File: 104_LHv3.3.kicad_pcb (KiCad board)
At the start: 2 copper layers, 436.9 x 129.9 mm, 229 parts, among them K1 CHRY_MX, K10 CHRY_MX, K100 CHRY_MX, K101 CHRY_MX, K102 CHRY_MX, K103 CHRY_MX, K104 CHRY_MX, K11 CHRY_MX, K12 CHRY_MX, K13 CHRY_MX, K14 CHRY_MX, K15 CHRY_MX, K16 CHRY_MX, K17 CHRY_MX, K18 CHRY_MX, K19 CHRY_MX, K2 CHRY_MX, K20 CHRY_MX, K21 CHRY_MX, K22 CHRY_MX, K23 CHRY_MX, K24 CHRY_MX, K25 CHRY_MX, K26 CHRY_MX, K27 CHRY_MX, K28 CHRY_MX, K29 CHRY_MX, K3 CHRY_MX, K30 CHRY_MX, K31 CHRY_MX, K32 CHRY_MX, K33 CHRY_MX, K34 CHRY_MX, K35 CHRY_MX, K36 CHRY_MX, K37 CHRY_MX, K38 CHRY_MX, K39 CHRY_MX, K4 CHRY_MX, K40 CHRY_MX, K41 CHRY_MX, K42 CHRY_MX, K43 CHRY_MX, K44 CHRY_MX, K45 CHRY_MX, K46 CHRY_MX, K47 CHRY_MX, K48 CHRY_MX, K49 CHRY_MX, K5 CHRY_MX, K50 CHRY_MX, K51 CHRY_MX, K52 CHRY_MX, K53 CHRY_MX, K54 CHRY_MX, K55 CHRY_MX, K56 CHRY_MX, K57 CHRY_MX, K58 CHRY_MX, K59 CHRY_MX, K6 CHRY_MX, K60 CHRY_MX, K61 CHRY_MX, K62 CHRY_MX, K63 CHRY_MX, K64 CHRY_MX, K65 CHRY_MX, K66 CHRY_MX, K67 CHRY_MX, K68 CHRY_MX, K69 CHRY_MX, K7 CHRY_MX, K70 CHRY_MX, K71 CHRY_MX, K72 CHRY_MX, K73 CHRY_MX, K74 CHRY_MX, K75 CHRY_MX, K76 CHRY_MX, K77 CHRY_MX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

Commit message: Add files via upload
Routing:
- net /COL_10: track 371.0 -> 348.4 mm
- net /SELECT: track 169.8 -> 152.6 mm, vias 2 -> 4
- net /COL_04: track 185.0 -> 177.8 mm
- net /GND: track 366.3 -> 359.1 mm, vias 33 -> 32
- net /COL_13: track 390.6 -> 384.7 mm
- net /COL_17: track 459.2 -> 464.9 mm
- net /COL_16: track 422.6 -> 427.0 mm
- net /ROW_04: track 510.4 -> 506.4 mm
- net /COL_05: track 191.2 -> 193.3 mm
- net /COL_14: track 397.7 -> 399.5 mm
- net /COL_21: track 531.0 -> 532.7 mm
- net /COL_20: track 525.6 -> 527.2 mm
- net /COL_19: track 459.1 -> 460.3 mm
- net /COL_07: track 256.6 -> 257.8 mm
- net /COL_15: track 420.8 -> 419.8 mm
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
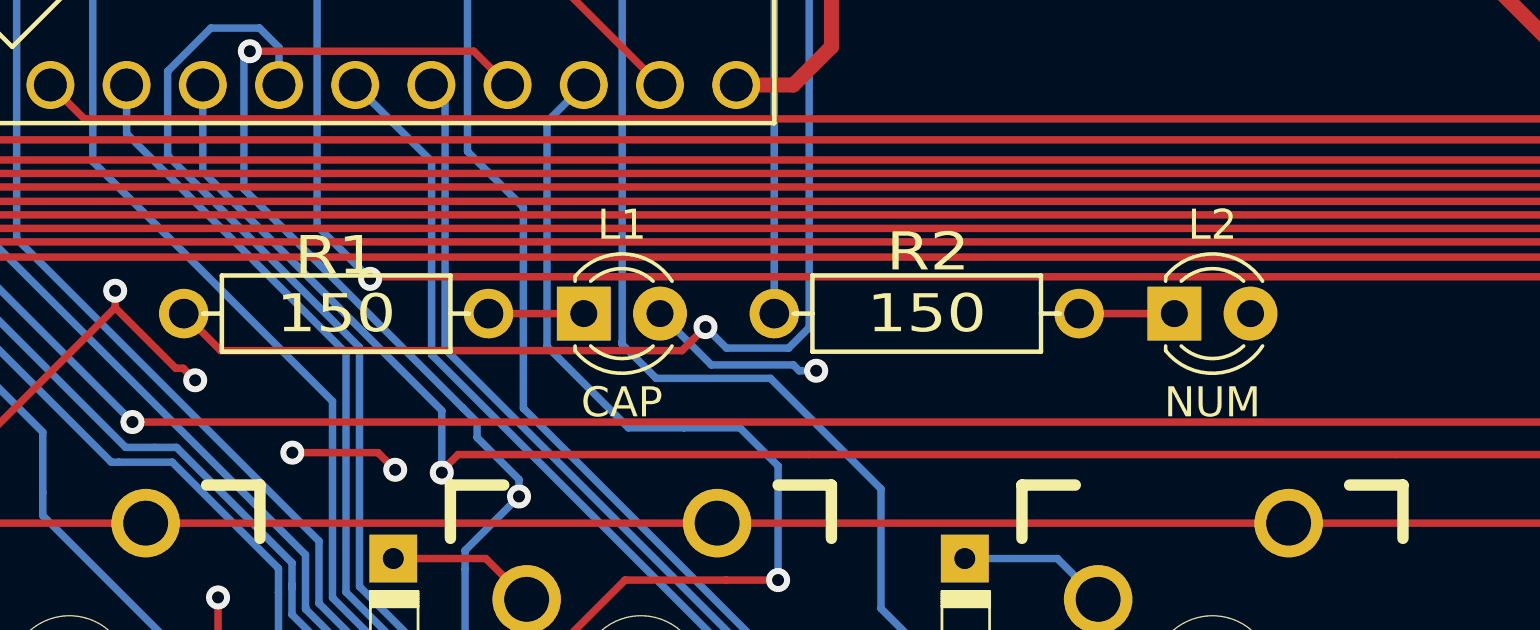
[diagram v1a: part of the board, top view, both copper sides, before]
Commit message: Fixed backwards LEDs
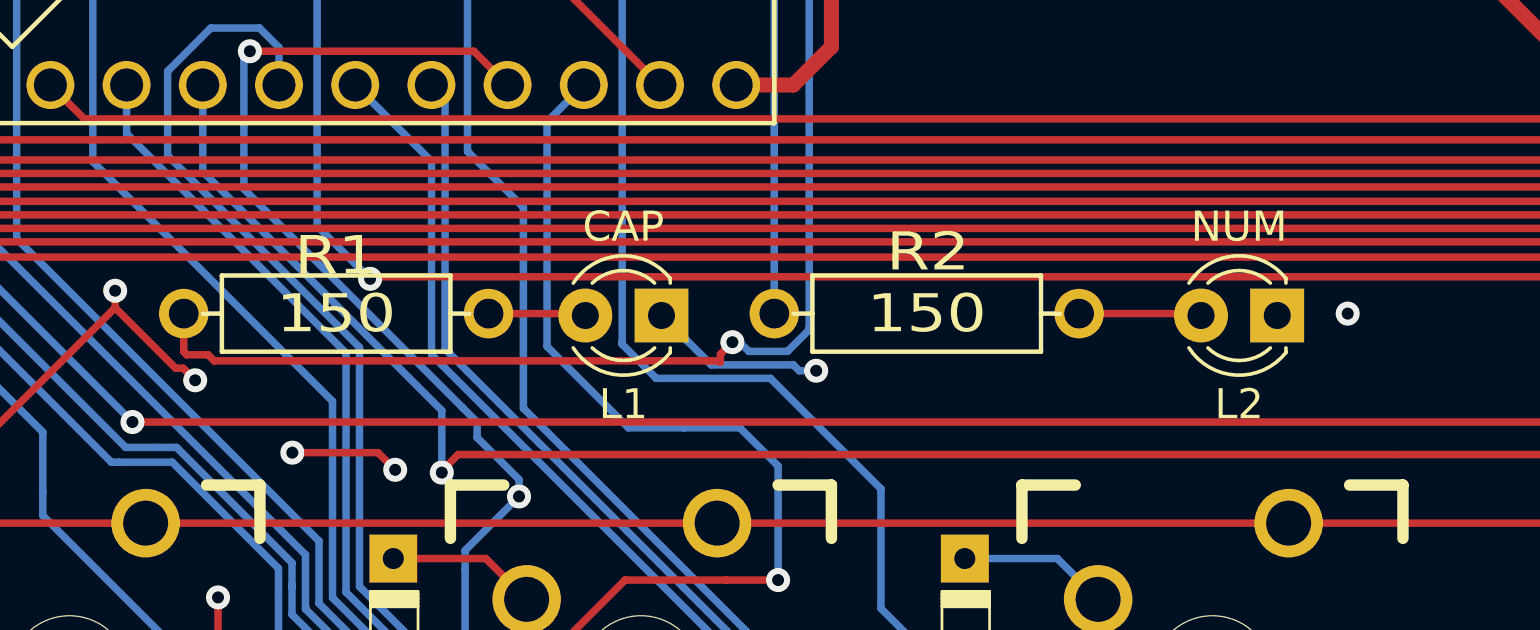
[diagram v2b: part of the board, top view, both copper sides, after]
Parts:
- moved L2 3.43 mm to (127.9, 109.3), turned to 180 degrees
- moved L1 2.59 mm to (107.4, 109.3), turned to 180 degrees
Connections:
- L1 pad 1: /R1 -> /GND
- L1 pad 2: /GND -> /R1
- L2 pad 1: /R2 -> /GND
- L2 pad 2: /GND -> /R2
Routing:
- net /LED_00: track 47.6 -> 48.6 mm
- net /GND: vias 32 -> 33
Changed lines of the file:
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@@
     (thickness 1.6)
     (drawings 43)
-    (tracks 1490)
+    (tracks 1498)
     (zones 0)
     (modules 229)
@@
   )
   (module pcb:LED_D3.0mm_FlatTop (layer F.Cu)
-    (at 124.46 109.22)
+    (at 127.889 109.2835 180)
     (descr "LED, Round, FlatTop, diameter 3.0mm, 2 pins, http://www.kingbright.com/attachments/file/psearch/000/00/00/L-47XEC(Ver.9A).pdf")
     (tags "LED Round FlatTop diameter 3.0mm 2 pins")
-    (fp_text reference L2 (at 1.27 -2.96) (layer F.SilkS)
+    (fp_text reference L2 (at 1.27 -2.96 180) (layer F.SilkS)
       (effects (font (size 1 1) (thickness 0.15)))
     )
-    (fp_text value NUM (at 1.27 2.96) (layer F.SilkS)
+    (fp_text value NUM (at 1.27 2.96 180) (layer F.SilkS)
       (effects (font (size 1 1) (thickness 0.15)))
     )
@@
     (fp_line (start 3.7 2.25) (end 3.7 -2.25) (layer F.CrtYd) (width 0.05))
     (fp_line (start 3.7 -2.25) (end -1.15 -2.25) (layer F.CrtYd) (width 0.05))
-    (pad 1 thru_hole rect (at 0 0) (size 1.8 1.8) (drill 0.9) (layers *.Cu *.Mask)
-      (net 141 /R2))
-    (pad 2 thru_hole circle (at 2.54 0) (size 1.8 1.8) (drill 0.9) (layers *.Cu *.Mask)
+    (pad 1 thru_hole rect (at 0 0 180) (size 1.8 1.8) (drill 0.9) (layers *.Cu *.Mask)
       (net 127 /GND))
+    (pad 2 thru_hole circle (at 2.54 0 180) (size 1.8 1.8) (drill 0.9) (layers *.Cu *.Mask)
+      (net 141 /R2))
   )
   (module pcb:LED_D3.0mm_FlatTop (layer F.Cu)
-    (at 104.775 109.22)
+    (at 107.3658 109.2835 180)
     (descr "LED, Round, FlatTop, diameter 3.0mm, 2 pins, http://www.kingbright.com/attachments/file/psearch/000/00/00/L-47XEC(Ver.9A).pdf")
     (tags "LED Round FlatTop diameter 3.0mm 2 pins")
-    (fp_text reference L1 (at 1.27 -2.96) (layer F.SilkS)
+    (fp_text reference L1 (at 1.27 -2.96 180) (layer F.SilkS)
       (effects (font (size 1 1) (thickness 0.15)))
     )
-    (fp_text value CAP (at 1.27 2.96) (layer F.SilkS)
+    (fp_text value CAP (at 1.27 2.96 180) (layer F.SilkS)
       (effects (font (size 1 1) (thickness 0.15)))
     )
@@
     (fp_arc (start 1.27 0) (end -0.29 -1.235516) (angle 108.8) (layer F.SilkS) (width 0.12))
     (fp_arc (start 1.27 0) (end -0.23 -1.16619) (angle 284.3) (layer F.Fab) (width 0.1))
-    (pad 2 thru_hole circle (at 2.54 0) (size 1.8 1.8) (drill 0.9) (layers *.Cu *.Mask)
-      (net 127 /GND))
-    (pad 1 thru_hole rect (at 0 0) (size 1.8 1.8) (drill 0.9) (layers *.Cu *.Mask)
+    (pad 2 thru_hole circle (at 2.54 0 180) (size 1.8 1.8) (drill 0.9) (layers *.Cu *.Mask)
       (net 140 /R1))
+    (pad 1 thru_hole rect (at 0 0 180) (size 1.8 1.8) (drill 0.9) (layers *.Cu *.Mask)
+      (net 127 /GND))
   )
   (module pcb:RESISTOR (layer F.Cu)
@@
   (gr_line (start 131.192 77.78) (end 121.868 77.78) (layer Edge.Cuts) (width 0.15))
   (gr_arc (start 134.73 83.33) (end 131.98 83.33) (angle -180) (layer Edge.Cuts) (width 0.15))
+  (via (at 130.2385 109.22) (size 0.8) (drill 0.4) (layers F.Cu B.Cu) (net 127))
   (segment (start 138.2724 102.7298) (end 138.2366 102.694) (width 0.25) (layer B.Cu) (net 1))
   (segment (start 144.78 97.245) (end 143.7572 97.245) (width 0.25) (layer B.Cu) (net 1))
@@
   (segment (start 107.315 86.36) (end 112.2874 91.3324) (width 0.25) (layer B.Cu) (net 143))
   (segment (start 112.2874 91.3324) (end 112.2874 109.6852) (width 0.25) (layer B.Cu) (net 143))
-  (segment (start 112.2874 109.6852) (end 111.6018 110.3708) (width 0.25) (layer B.Cu) (net 143))
-  (segment (start 111.6018 110.3708) (end 109.5324 110.3708) (width 0.25) (layer B.Cu) (net 143))
-  (segment (start 109.5324 110.3708) (end 108.8312 109.6696) (width 0.25) (layer B.Cu) (net 143))
-  (segment (start 108.8312 109.6696) (end 108.0469 110.4539) (width 0.25) (layer F.Cu) (net 143))
-  (segment (start 108.0469 110.4539) (end 92.6739 110.4539) (width 0.25) (layer F.Cu) (net 143))
-  (segment (start 92.6739 110.4539) (end 91.44 109.22) (width 0.25) (layer F.Cu) (net 143))
-  (via (at 108.8312 109.6696) (size 0.8) (layers F.Cu B.Cu) (net 143))
+  (via (at 109.728 110.1725) (size 0.8) (layers F.Cu B.Cu) (net 143))
+  (segment (start 112.2874 109.760342) (end 111.568762 110.47898) (width 0.25) (layer B.Cu) (net 143))
+  (segment (start 112.2874 109.6852) (end 112.2874 109.760342) (width 0.25) (layer B.Cu) (net 143))
+  (segment (start 109.728 110.1725) (end 109.9693 110.1725) (width 0.25) (layer B.Cu) (net 143))
+  (segment (start 109.9693 110.1725) (end 110.27578 110.47898) (width 0.25) (layer B.Cu) (net 143))
+  (segment (start 110.27578 110.47898) (end 111.5568 110.47898) (width 0.25) (layer B.Cu) (net 143))
+  (segment (start 109.328001 110.572499) (end 109.328001 110.839199) (width 0.25) (layer F.Cu) (net 143))
+  (segment (start 109.728 110.1725) (end 109.328001 110.572499) (width 0.25) (layer F.Cu) (net 143))
+  (segment (start 109.328001 110.839199) (end 109.283602 110.7948) (width 0.25) (layer F.Cu) (net 143))
+  (segment (start 109.283602 110.7948) (end 92.456 110.7948) (width 0.25) (layer F.Cu) (net 143))
+  (segment (start 92.253692 110.592492) (end 91.542492 110.592492) (width 0.25) (layer F.Cu) (net 143))
+  (segment (start 92.456 110.7948) (end 92.253692 110.592492) (width 0.25) (layer F.Cu) (net 143))
+  (segment (start 91.542492 110.592492) (end 91.44 110.49) (width 0.25) (layer F.Cu) (net 143))
+  (segment (start 91.44 110.49) (end 91.44 109.22) (width 0.25) (layer F.Cu) (net 143))
   (segment (start 104.775 86.36) (end 111.125 92.71) (width 0.25) (layer B.Cu) (net 144))
   (segment (start 111.125 92.71) (end 111.125 109.22) (width 0.25) (layer B.Cu) (net 144))

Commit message: Clean up LED text
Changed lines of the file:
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@@
   )
   (layers
-    (0 F.Cu signal)
-    (31 B.Cu signal)
+    (0 F.Cu signal hide)
+    (31 B.Cu signal hide)
     (32 B.Adhes user)
     (33 F.Adhes user)
@@
     (descr "LED, Round, FlatTop, diameter 3.0mm, 2 pins, http://www.kingbright.com/attachments/file/psearch/000/00/00/L-47XEC(Ver.9A).pdf")
     (tags "LED Round FlatTop diameter 3.0mm 2 pins")
-    (fp_text reference L2 (at 1.27 -2.96 180) (layer F.SilkS)
+    (fp_text reference L2 (at 1.143 2.8575 180) (layer F.SilkS)
       (effects (font (size 1 1) (thickness 0.15)))
     )
-    (fp_text value NUM (at 1.27 2.96 180) (layer F.SilkS)
+    (fp_text value NUM (at 1.143 -2.7305 180) (layer F.SilkS)
       (effects (font (size 1 1) (thickness 0.15)))
     )
@@
     (descr "LED, Round, FlatTop, diameter 3.0mm, 2 pins, http://www.kingbright.com/attachments/file/psearch/000/00/00/L-47XEC(Ver.9A).pdf")
     (tags "LED Round FlatTop diameter 3.0mm 2 pins")
-    (fp_text reference L1 (at 1.27 -2.96 180) (layer F.SilkS)
+    (fp_text reference L1 (at 1.27 2.8575 180) (layer F.SilkS)
       (effects (font (size 1 1) (thickness 0.15)))
     )
-    (fp_text value CAP (at 1.27 2.96 180) (layer F.SilkS)
+    (fp_text value CAP (at 1.3208 -2.7305 180) (layer F.SilkS)
       (effects (font (size 1 1) (thickness 0.15)))
     )
@@
   (gr_line (start 131.192 77.78) (end 121.868 77.78) (layer Edge.Cuts) (width 0.15))
   (gr_arc (start 134.73 83.33) (end 131.98 83.33) (angle -180) (layer Edge.Cuts) (width 0.15))
-  (via (at 130.2385 109.22) (size 0.8) (drill 0.4) (layers F.Cu B.Cu) (net 127))
   (segment (start 138.2724 102.7298) (end 138.2366 102.694) (width 0.25) (layer B.Cu) (net 1))
   (segment (start 144.78 97.245) (end 143.7572 97.245) (width 0.25) (layer B.Cu) (net 1))
@@
   (segment (start 478.93 194.945) (end 476.8303 194.945) (width 0.25) (layer B.Cu) (net 126))
   (segment (start 476.8303 194.945) (end 475.4703 193.585) (width 0.25) (layer B.Cu) (net 126))
+  (via (at 130.2385 109.22) (size 0.8) (drill 0.4) (layers F.Cu B.Cu) (net 127))
   (via (at 98.4885 114.427) (size 0.8) (drill 0.4) (layers F.Cu B.Cu) (net 127))
   (via (at 95.0595 113.8555) (size 0.8) (drill 0.4) (layers F.Cu B.Cu) (net 127))

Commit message: Cleaning up tracks
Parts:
- SJ1: value Solder_Jumper -> Jumper
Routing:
- net /COL_10: track 348.4 -> 331.5 mm
- net /COL_09: track 295.9 -> 280.7 mm
- net /GND: track 359.1 -> 366.4 mm, vias 33 -> 35
- net /COL_20: track 527.2 -> 526.1 mm
- net /COL_00: track 142.1 -> 143.2 mm
- net /COL_11: track 323.3 -> 324.1 mm
- net /COL_12: track 345.3 -> 346.0 mm
- net /COL_17: track 464.9 -> 465.6 mm
- net /COL_18: track 477.6 -> 478.3 mm
- net /COL_15: track 419.8 -> 420.4 mm
- net /COL_13: track 384.7 -> 385.4 mm
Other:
- board size 436.9 x 129.9 mm -> 437.5 x 129.9 mm

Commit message: Adding support for Stabilizers.
Prototype boards have been ordered. If they work as intended, this version will be the next batch ordered with Cherry MX Stabilizer support.
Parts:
- added >NAME: >VALUE, mx_stabs:Mx_Stab_625, F.Cu at (339.9, 197.5)
- added G***: LOGO, logo:logoR, F.Cu at (373.4, 197.2)
- added G***: LOGO, logo:logo, F.Cu at (305.8, 198.6)
- moved REF** 6.60 mm to (348.7, 205.6)
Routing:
- net /GND: track 366.4 -> 370.0 mm, vias 35 -> 36
- net /COL_05: track 193.3 -> 195.5 mm
- net /COL_07: track 257.8 -> 259.4 mm
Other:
- board size 437.5 x 129.9 mm -> 437.5 x 130.6 mm
- board text added: "PROTOTYPE"

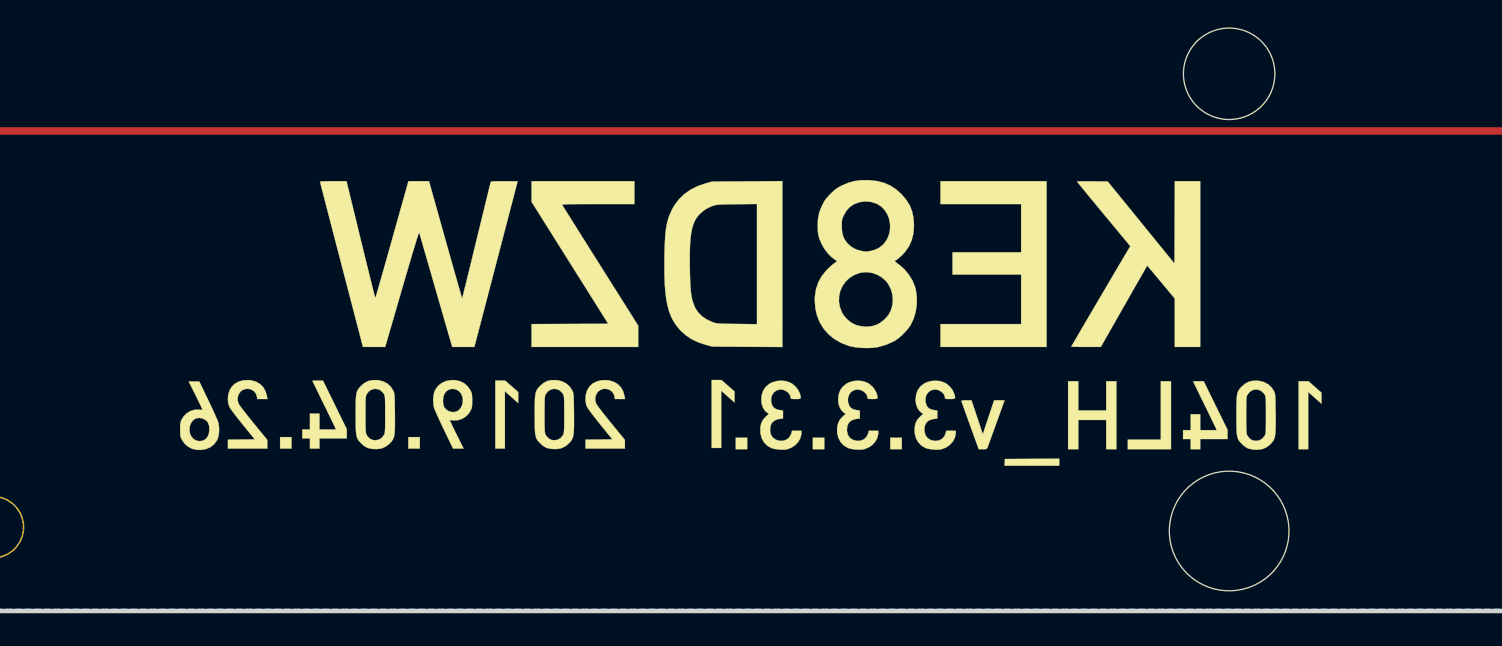
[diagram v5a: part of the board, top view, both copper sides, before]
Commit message: Clean up. Support for Cherry MX Stabilizers.
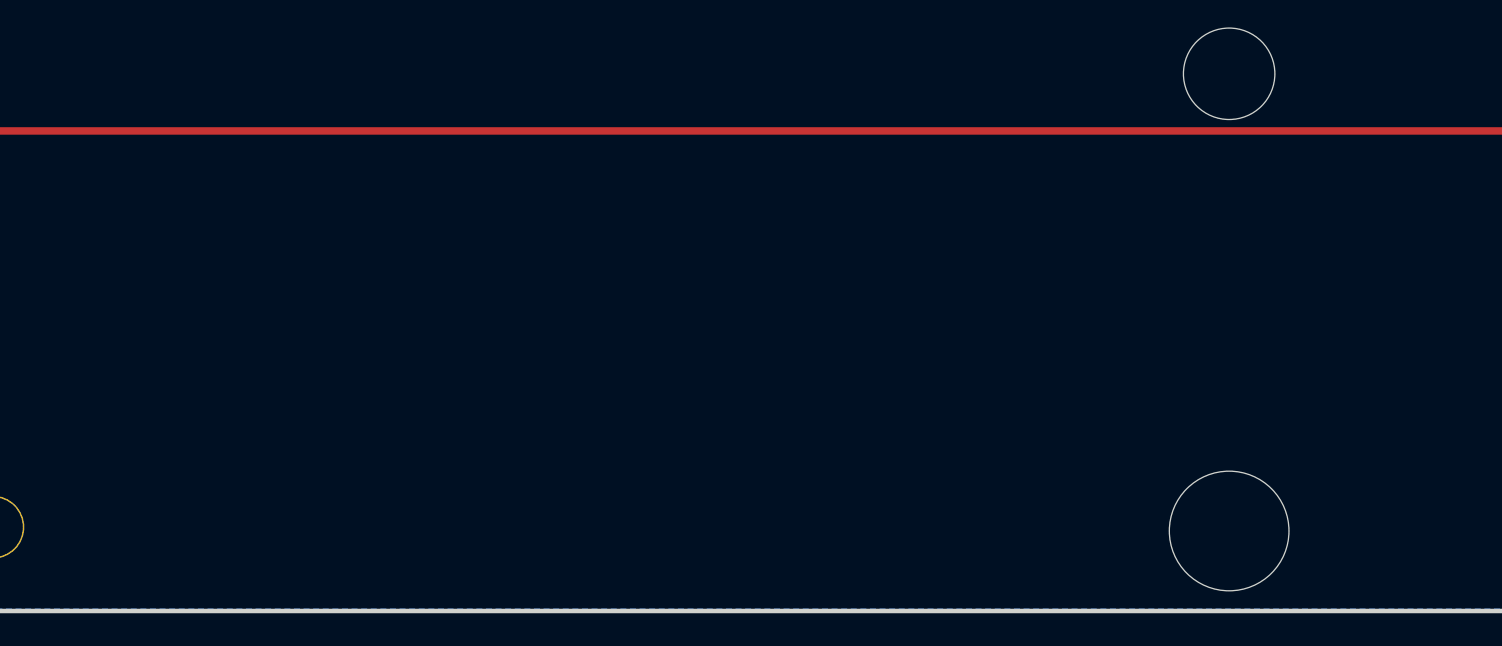
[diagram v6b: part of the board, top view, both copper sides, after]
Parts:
- moved G*** 6.53 mm to (366.9, 197.1)

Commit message: Adding more stabilizers
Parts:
- added >NAME: >VALUE, mx_stabs:Mx_Stab_275, F.Cu at (468.5, 178.4)
- added >NAME: >VALUE, mx_stabs:Mx_Stab_225, F.Cu at (473.3, 159.4)
- added >NAME: >VALUE, mx_stabs:Mx_Stab_225, F.Cu at (230.4, 178.4)
- added ST72: Stabilizer, mx_stabs:Mx_Stab_200, F.Cu at (68.6, 188.0)
- added ST72: Stabilizer, mx_stabs:Mx_Stab_200, F.Cu at (68.6, 149.9)
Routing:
- net /GND: track 370.0 -> 395.7 mm, vias 36 -> 41
- net /COL_00: track 143.2 -> 150.1 mm
- net /COL_01: track 144.4 -> 138.9 mm, vias 1 -> 2
- net /COL_20: track 526.1 -> 528.6 mm
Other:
- board size 437.5 x 130.6 mm -> 437.8 x 130.6 mm

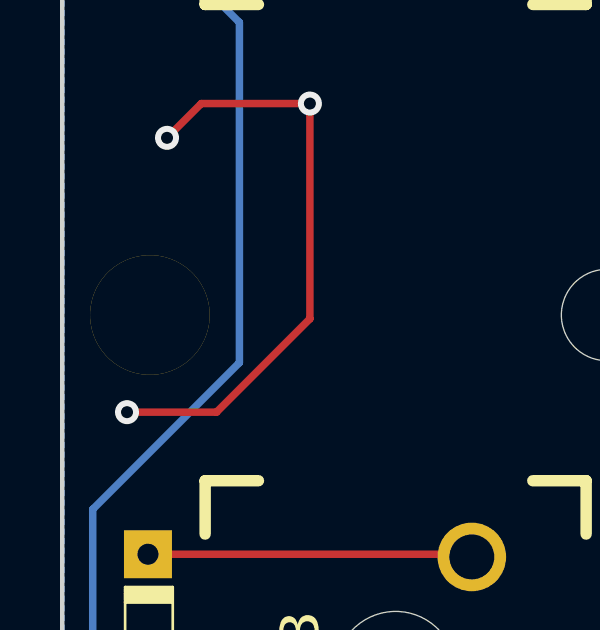
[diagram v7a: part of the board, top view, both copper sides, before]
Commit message: Stabilizers added.
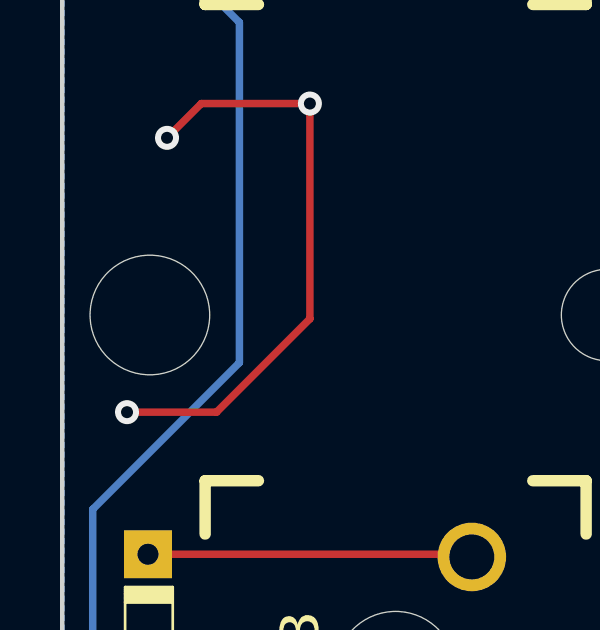
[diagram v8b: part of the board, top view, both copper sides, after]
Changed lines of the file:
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@@
     (pad "" np_thru_hole circle (at -11.938 -6.985 270) (size 3.048 3.048) (drill 3.048) (layers *.Cu *.Mask))
     (pad "" np_thru_hole circle (at 11.938 -6.985 270) (size 3.048 3.048) (drill 3.048) (layers *.Cu *.Mask))
-    (pad "" thru_hole circle (at -11.938 8.255 270) (size 3.9878 3.9878) (drill 3.9878) (layers *.Cu *.Mask))
+    (pad "" np_thru_hole circle (at -11.938 8.255 270) (size 3.9878 3.9878) (drill 3.9878) (layers *.Cu *.Mask))
     (pad "" np_thru_hole circle (at 11.938 8.255 270) (size 3.9878 3.9878) (drill 3.9878) (layers *.Cu *.Mask))
   )
